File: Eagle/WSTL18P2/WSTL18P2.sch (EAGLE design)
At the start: 24 parts, among them CON1 1X6CONN-1.27-ROUND_CENTERED, CON2 1X6CONN-1.27-ROUND_CENTERED, CON3 1X6CONN-1.27-ROUND_CENTERED, CON4 1X6CONN-1.27-ROUND_CENTERED, T1 ABS07AIG

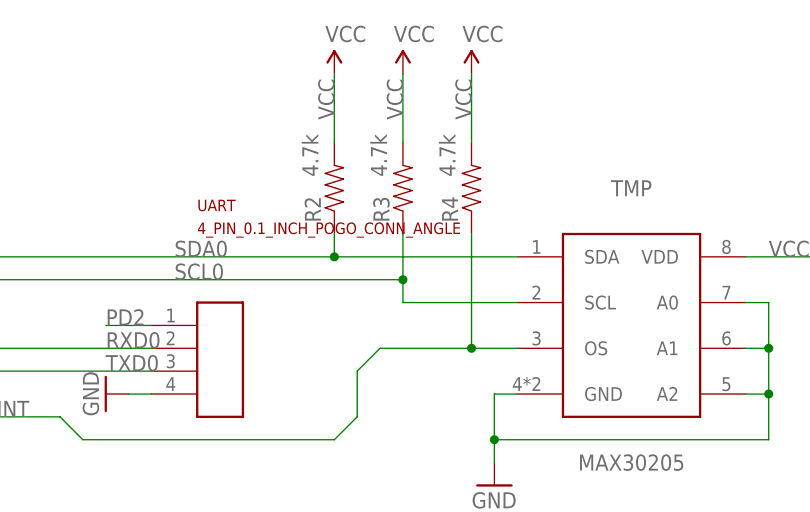
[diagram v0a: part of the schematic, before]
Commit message: Removed a couple of diagrams to reorganize them
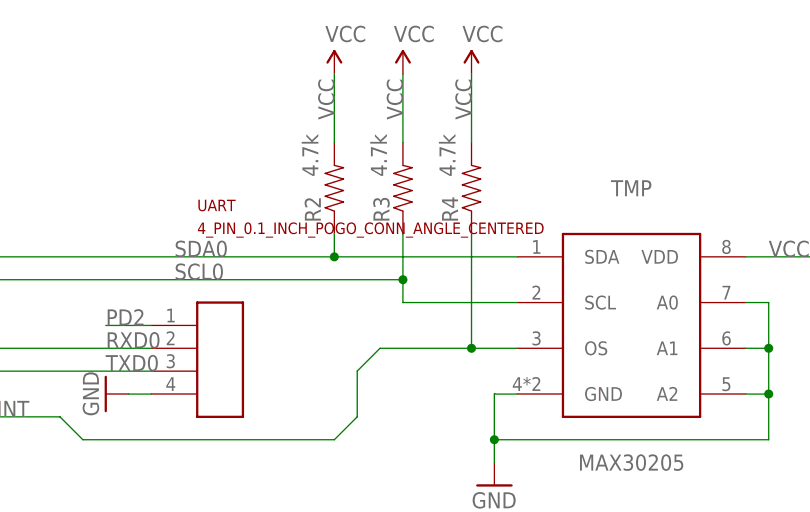
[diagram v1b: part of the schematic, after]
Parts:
- UART: value 4_PIN_0.1_INCH_POGO_CONN_ANGLE -> 4_PIN_0.1_INCH_POGO_CONN_ANGLE_CENTERED; device Connectors:4_PIN_0.1_INCH_POGO_CONN_ANGLE -> Connectors:4_PIN_0.1_INCH_POGO_CONN_ANGLE_CENTERED
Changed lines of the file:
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@@
 <part name="VCC4" library="SparkFun-Aesthetics" deviceset="5V" device="" value="VCC"/>
 <part name="VCC7" library="SparkFun-Aesthetics" deviceset="5V" device="" value="VCC"/>
-<part name="UART" library="Connectors" deviceset="4_PIN_0.1_INCH_POGO_CONN_ANGLE" device=""/>
+<part name="UART" library="Connectors" deviceset="4_PIN_0.1_INCH_POGO_CONN_ANGLE_CENTERED" device=""/>
 <part name="U$1" library="Battery_holders" deviceset="LINX-CR2032-BAT-HLD-M-THM" device=""/>
 <part name="C6" library="Passives" deviceset="CAP_0402_CERAMIC" device=""/>
